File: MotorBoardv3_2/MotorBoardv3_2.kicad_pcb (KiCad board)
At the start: 2 copper layers, 128.3 x 129.5 mm, 84 parts, among them J1 Bump0, J10 RxD, J11 GP2Y0A41SK0F, J12 GP2Y0A41SK0F, J13 GP2Y0A41SK0F, J14 TxD, J15 7.2, J16 LP5.0, J17 ELA, J18 ERA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

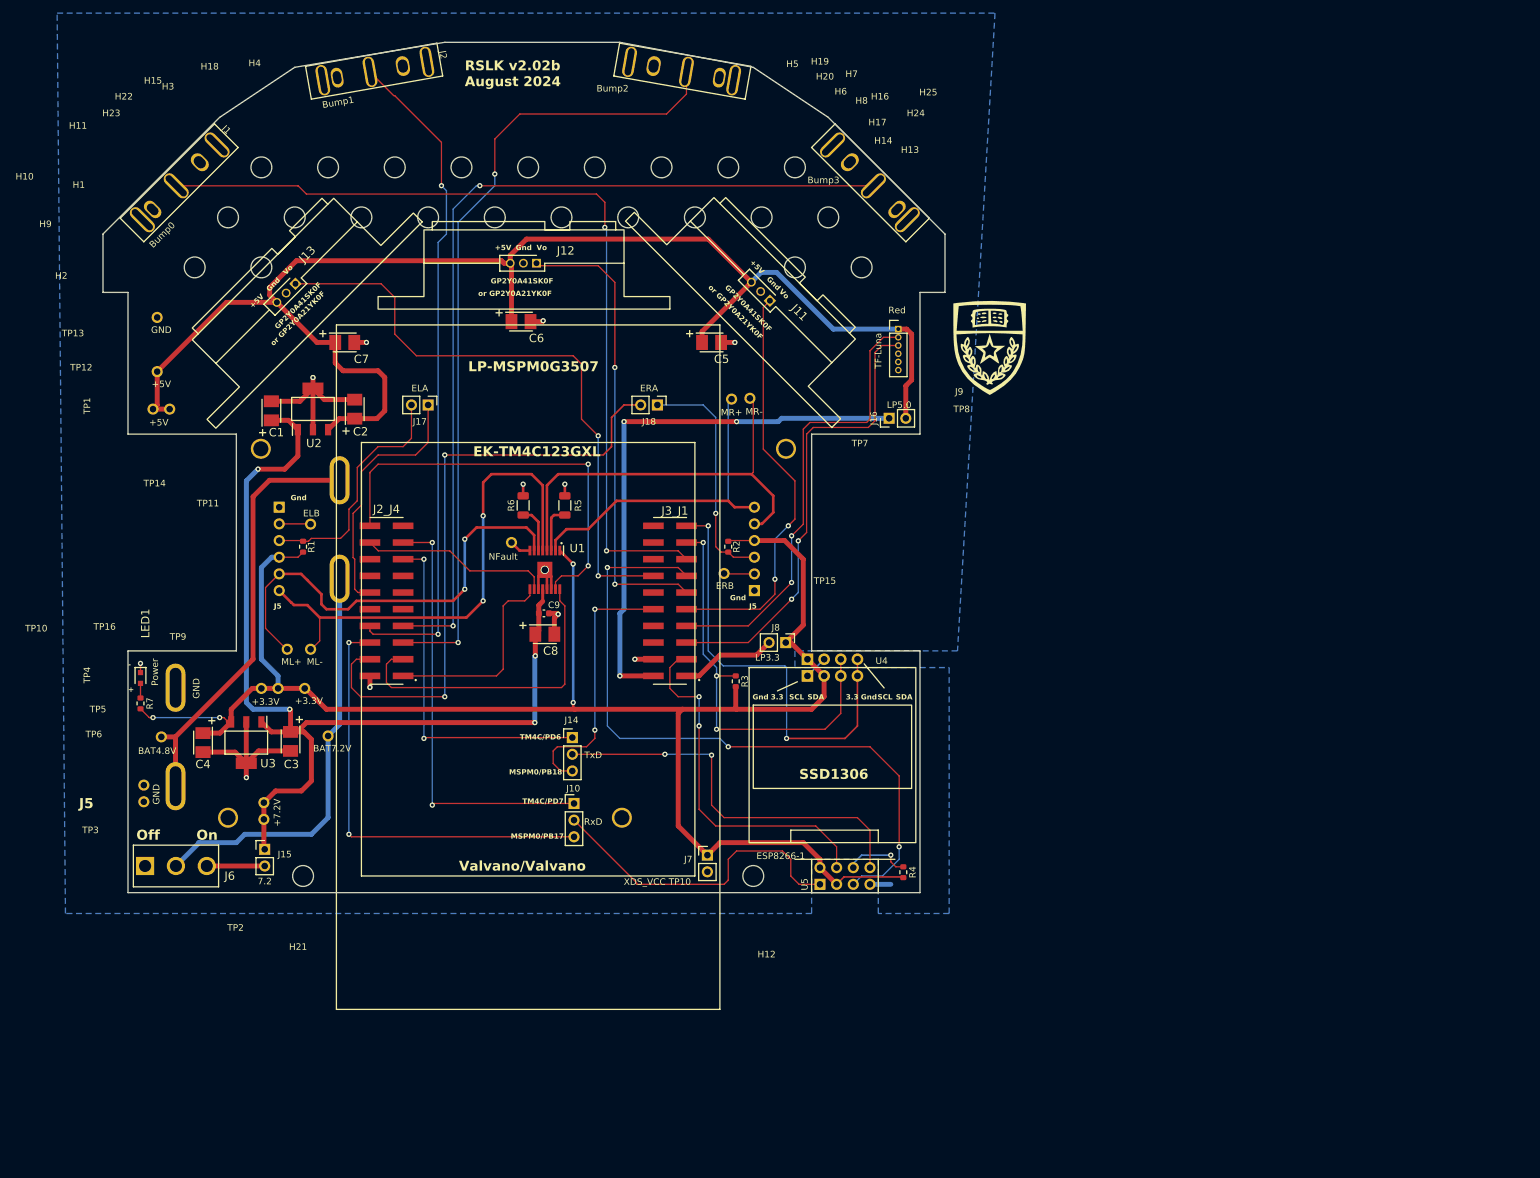
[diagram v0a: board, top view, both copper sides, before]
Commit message: Added voltage display
Modified schematic and layout to include voltage display. Expanded board outline in layout to have more space at the back of the robot.
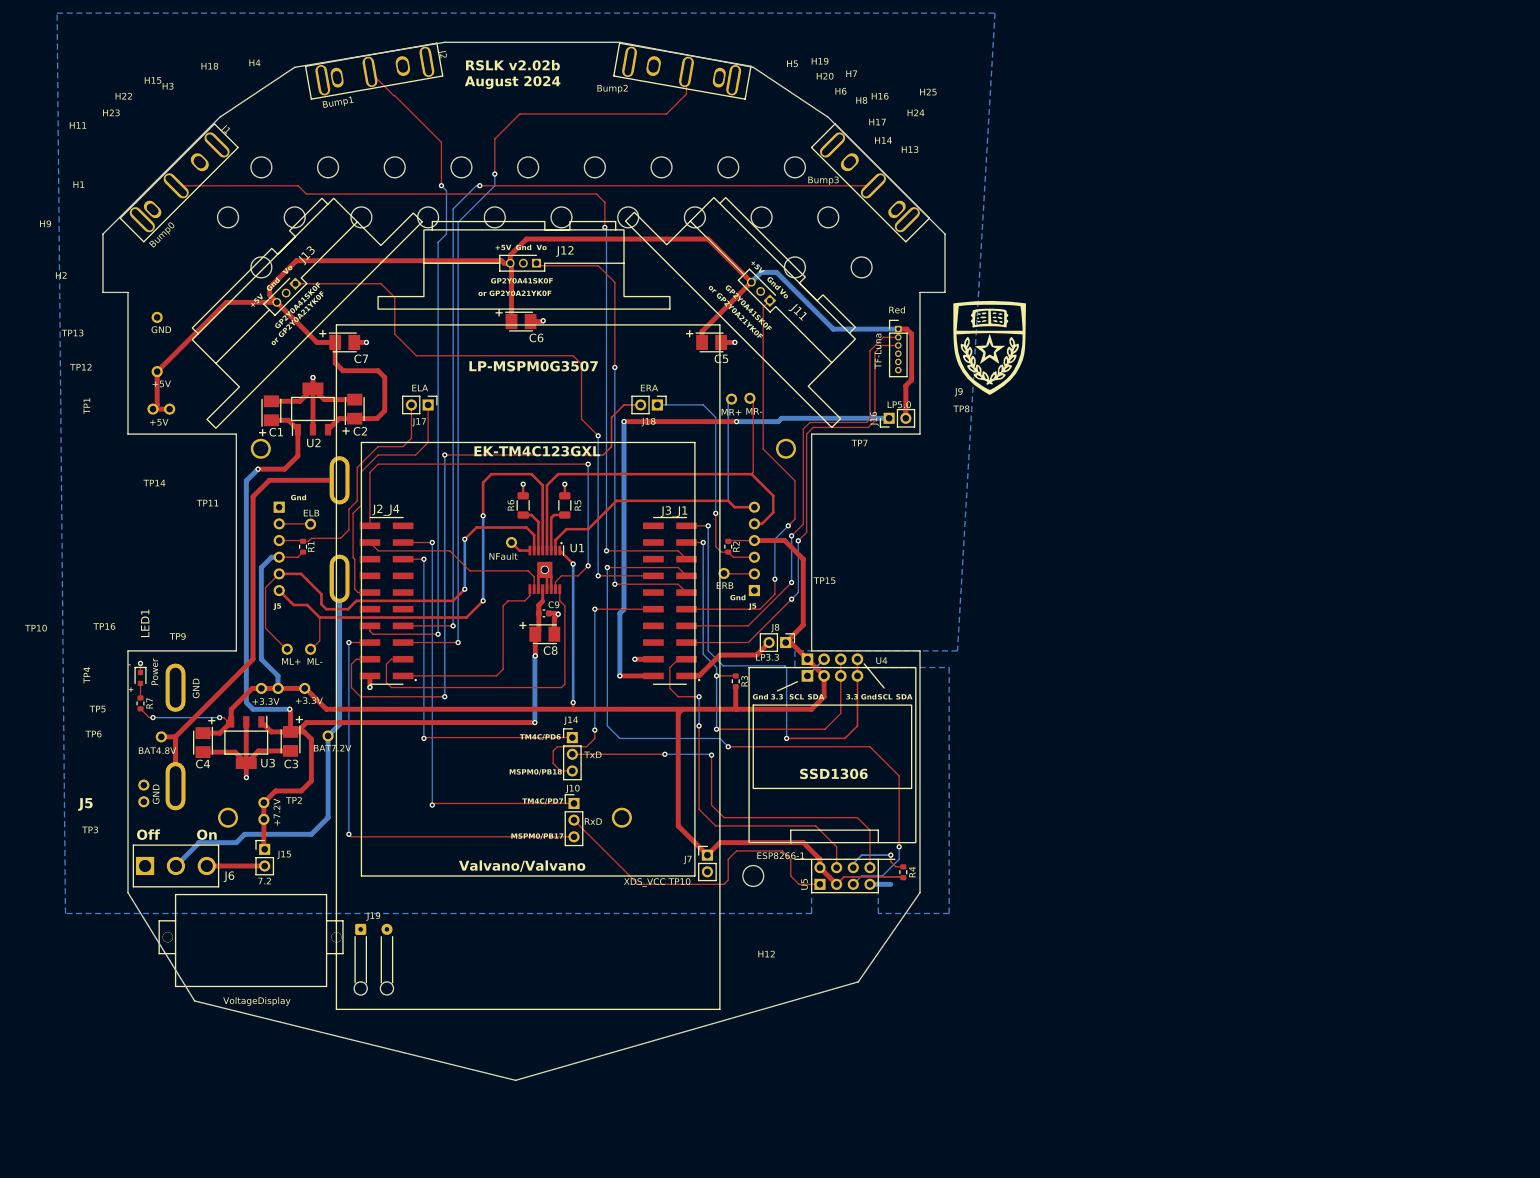
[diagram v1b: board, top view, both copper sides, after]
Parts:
- removed H10, H21: ~, RSLK2:MountingHole_4_40
- added J19: Voltage Display, Connector_Wire:SolderWire-0.15sqmm_1x02_P4mm_D0.5mm_OD1.5mm_Relief, F.Cu at (83.7, 159.3)
- added VoltageDisplay: PRT-14313, VoltageDisplay:PRT-14313, F.Cu at (55.5, 168.0)
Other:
- board size 128.3 x 129.5 mm -> 128.3 x 158.1 mm

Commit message: Deleted traces and text from ESP and Luna
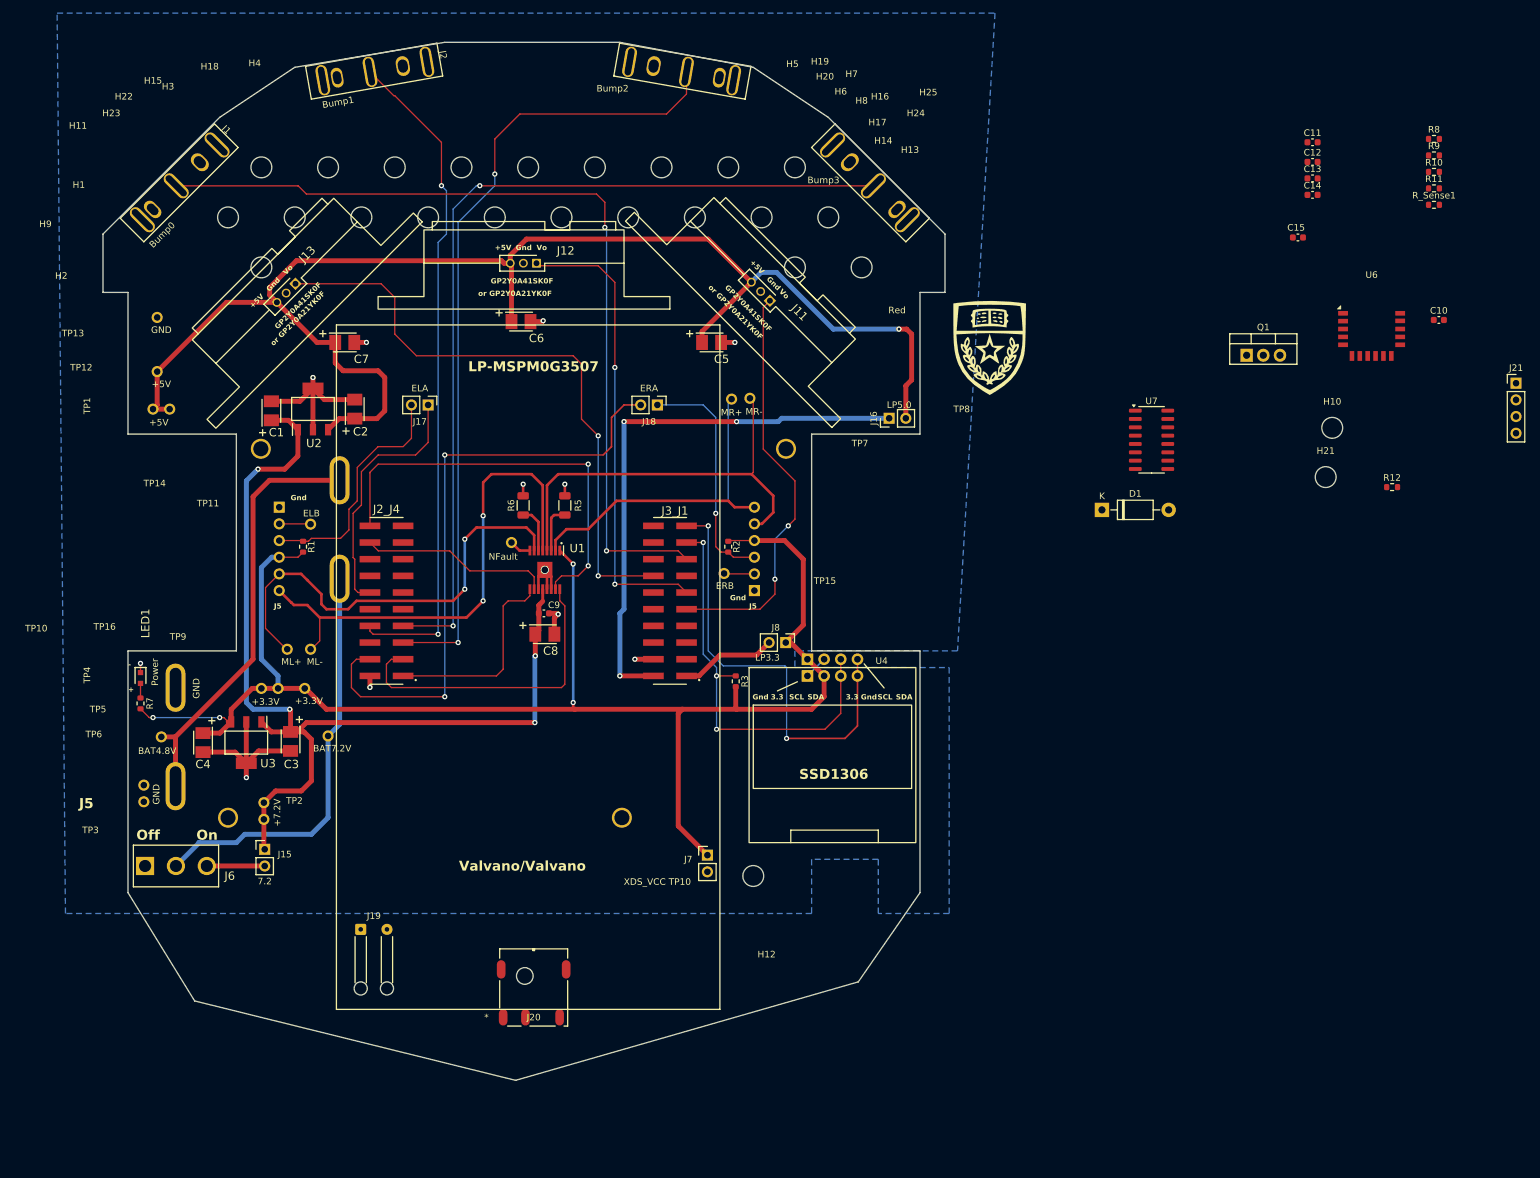
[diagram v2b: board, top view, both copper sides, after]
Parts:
- removed J10: RxD, RSLK2:PinHeader_1x03_P2.54mm_Vertical
- removed J14: TxD, RSLK2:PinHeader_1x03_P2.54mm_Vertical
- removed J9: TF-Luna, RSLK2:JST-GH_1x06_1.25mm
- removed R4: 10k, RSLK2:R_0603_1608Metric
- removed U5: ESP8266-1, RSLK2:PinHeader_2x04_P2.54mm_Vertical
- removed VoltageDisplay: PRT-14313, VoltageDisplay:PRT-14313
- added C10: 10uF, RSLK2:C_0603_1608Metric, F.Cu at (247.9, 66.4)
- added C11: 10uF, RSLK2:C_0603_1608Metric, F.Cu at (228.7, 39.4)
- added C12: 1uF, RSLK2:C_0603_1608Metric, F.Cu at (228.7, 42.4)
- added C13: 0.01uF, RSLK2:C_0603_1608Metric, F.Cu at (228.7, 44.9)
- added C14: 0.01uF, RSLK2:C_0603_1608Metric, F.Cu at (228.7, 47.4)
- added C15: 10uF, RSLK2:C_0603_1608Metric, F.Cu at (226.5, 53.9)
- added D1: 1N4001, Diode_THT:D_DO-41_SOD81_P10.16mm_Horizontal, F.Cu at (196.6, 95.4)
- added H10: ~, RSLK2:MountingHole_4_40, F.Cu at (231.7, 82.9)
- added H21: ~, RSLK2:MountingHole_4_40, F.Cu at (230.7, 90.4)
- added J20: Barrel_Jack, RSLK2:54-00127_TEN, F.Cu at (105.4, 172.7)
- added J21: Reflector I2C, Connector_PinHeader_2.54mm:PinHeader_1x04_P2.54mm_Vertical, F.Cu at (259.7, 76.1)
- added Q1: TIP42A, Package_TO_SOT_THT:TO-220-3_Vertical, F.Cu at (218.7, 71.8)
- added R10: 22K, RSLK2:R_0603_1608Metric, F.Cu at (247.2, 43.9)
- added R11: 150, RSLK2:R_0603_1608Metric, F.Cu at (247.2, 46.4)
- added R12: 1.5k, RSLK2:R_0603_1608Metric, F.Cu at (240.8, 91.9)
- added R8: 1.4k, RSLK2:R_0603_1608Metric, F.Cu at (247.2, 38.9)
- added R9: 68K, RSLK2:R_0603_1608Metric, F.Cu at (247.2, 41.4)
- added R_Sense1: 590m, RSLK2:R_0603_1608Metric, F.Cu at (247.2, 48.9)
- added U6: RN4871, RF_Module:Microchip_RN4871, F.Cu at (237.7, 68.9)
- added U7: MAX712CSE, Package_SO:SOIC-16_3.9x9.9mm_P1.27mm, F.Cu at (204.2, 84.7)
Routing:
- net PB9: track 105.6 -> 0.00 mm, vias 3 -> 0
- net PA9: track 70.5 -> 0.00 mm, vias 2 -> 0
- net PA8: track 69.2 -> 0.00 mm, vias 2 -> 0
- net PB17: track 66.9 -> 0.00 mm, vias 2 -> 0
- net PA12: track 66.1 -> 0.00 mm, vias 2 -> 0
- net /ESP_TxD: track 60.5 -> 0.00 mm, vias 2 -> 0
- net PA25: track 54.9 -> 1.27 mm, vias 2 -> 0
- net PA11: track 53.1 -> 0.00 mm, vias 2 -> 0
- net /ESP_RxD: track 49.2 -> 0.00 mm
- net PB18: track 41.0 -> 0.00 mm, vias 2 -> 0
- net +3V3: track 267.8 -> 233.3 mm
- net /Ch_PD: track 10.1 -> 0.00 mm, vias 1 -> 0
- net GND: track 83.2 -> 80.0 mm
- net +5V: vias 0 -> 1
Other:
- board text removed: "EK-TM4C123GXL"
- board text removed: "MSPM0/PB17"
- board text removed: "MSPM0/PB18"
- board text removed: "RSLK v2.02b August 2024"
- board text removed: "TM4C/PD6"
- board text removed: "TM4C/PD7"

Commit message: Fixed footprint not in library error
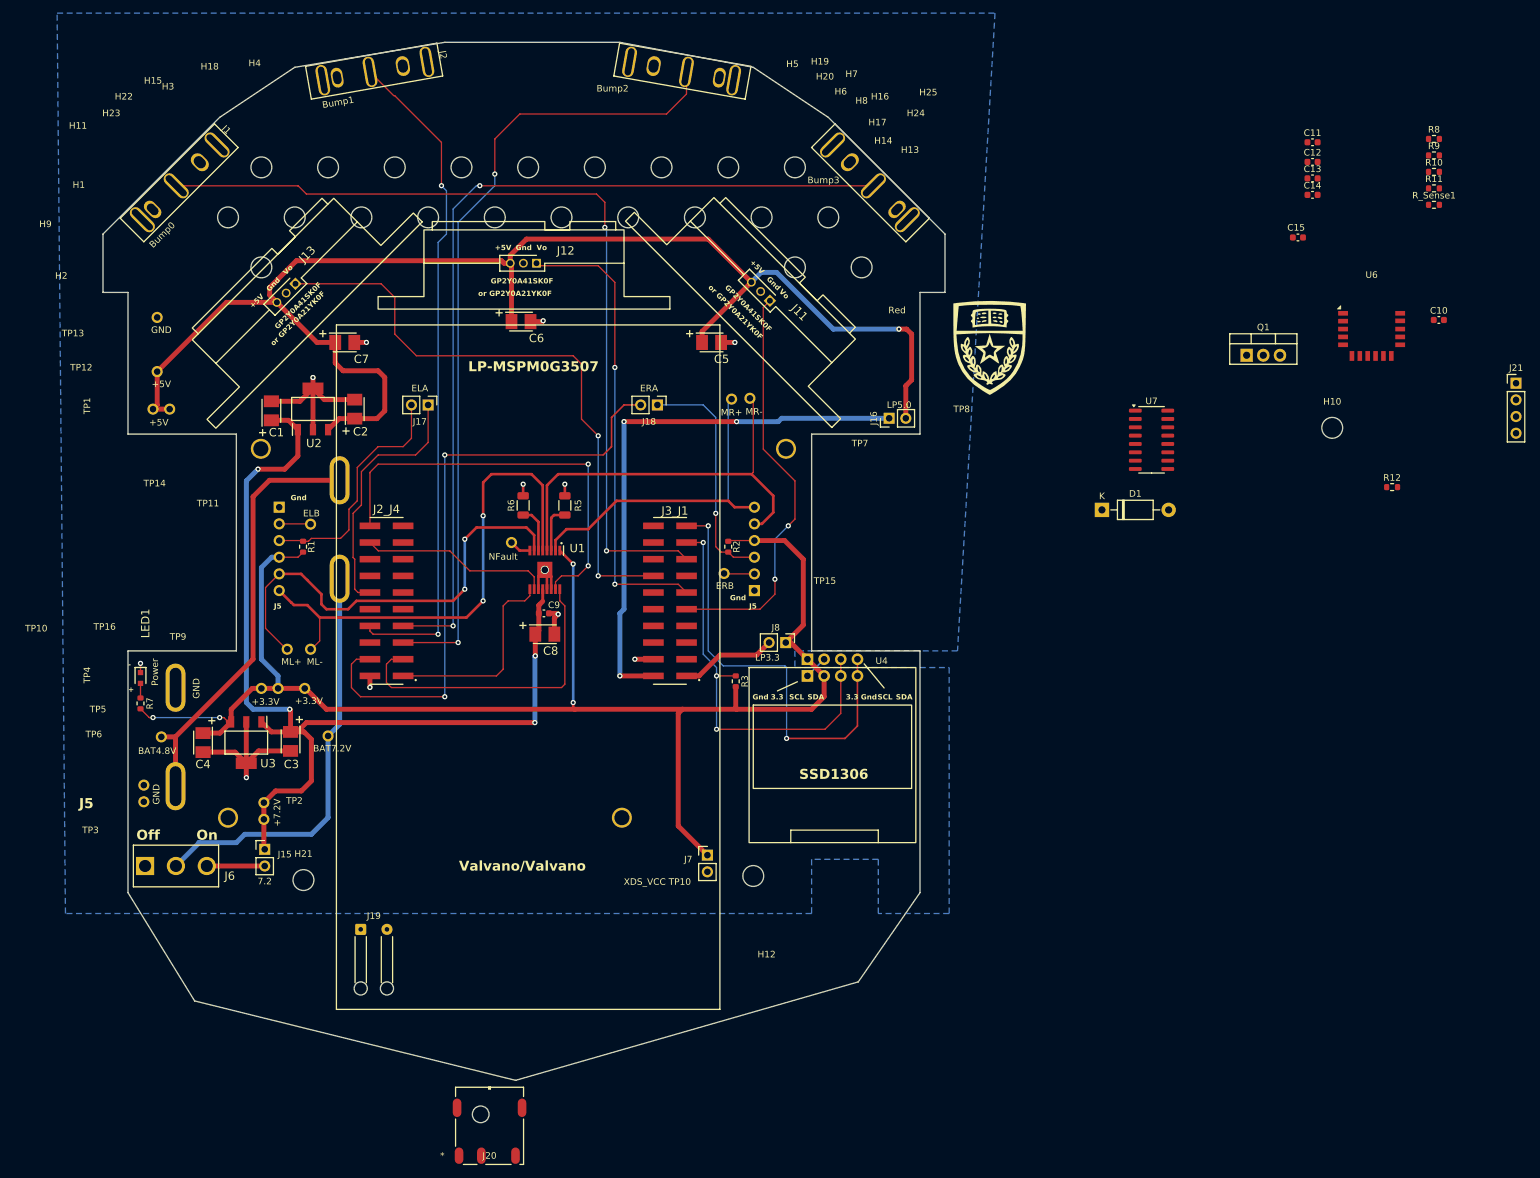
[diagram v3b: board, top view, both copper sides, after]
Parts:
- moved H21 167.4 mm to (75.0, 151.8)
- moved J20 22.1 mm to (98.7, 193.7)
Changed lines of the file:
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@@
 		)
 		(pad "4" thru_hole oval
-			(at 0 -6.260002 280)
+			(at 0 -6.260001 280)
 			(size 4.699 1.778)
 			(drill oval 4.191 1.016)
@@
 	(footprint "RSLK2:54-00127_TEN"
 		(layer "F.Cu")
-		(at 105.409999 172.659955)
+		(at 98.689999 193.739955)
 		(tags "54-00127 ")
 		(property "Reference" "J20"
@@
 	(footprint "RSLK2:MountingHole_4_40"
 		(layer "F.Cu")
-		(at 230.71 90.36)
+		(at 74.99 151.75)
 		(descr "Mounting Hole 0.125in")
 		(tags "mounting hole 0.125in 4_40")
@@
 		)
 		(property "Footprint" "RSLK2:D2F-01L30-D3_5pin"
-			(at 0 0 -135)
+			(at 0 0 45)
 			(layer "F.Fab")
 			(hide yes)
@@
 		)
 		(property "Datasheet" ""
-			(at 0 0 -135)
+			(at 0 0 45)
 			(layer "F.Fab")
 			(hide yes)
@@
 		)
 		(property "Description" "Bump switch"
-			(at 0 0 -135)
+			(at 0 0 45)
 			(layer "F.Fab")
 			(hide yes)
@@
 		(fp_poly
 			(pts
-				(xy -2.54 -8.89) (xy -7.62 -8.89) (xy -7.62 4.445) (xy -2.54 4.445)
+				(xy -7.62 4.445) (xy -2.54 4.445) (xy -2.54 -8.89) (xy -7.62 -8.89)
 			)
 			(stroke
@@
 		)
 		(property "Footprint" "RSLK2:D2F-01L30-D3_5pin"
-			(at 0 0 -100)
+			(at 0 0 80)
 			(layer "F.Fab")
 			(hide yes)
@@
 		)
 		(property "Datasheet" ""
-			(at 0 0 -100)
+			(at 0 0 80)
 			(layer "F.Fab")
 			(hide yes)
@@
 		)
 		(property "Description" "Bump switch"
-			(at 0 0 -100)
+			(at 0 0 80)
 			(layer "F.Fab")
 			(hide yes)
@@
 		(fp_poly
 			(pts
-				(xy -2.54 -8.89) (xy -7.62 -8.89) (xy -7.62 4.445) (xy -2.54 4.445)
+				(xy -7.62 4.445) (xy -2.54 4.445) (xy -2.54 -8.89) (xy -7.62 -8.89)
 			)
 			(stroke
@@
 		)
 		(pad "4" thru_hole oval
-			(at 0 6.260002 260)
+			(at 0 6.260001 260)
 			(size 4.699 1.778)
 			(drill oval 4.191 1.016)
